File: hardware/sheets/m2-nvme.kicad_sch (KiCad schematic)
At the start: 20 parts, among them J50 M.2 M-key, M2 CM5002016 (J2), SW3 door microswitch, U50 TPS22965DSGR, U51 AP63203WU-7

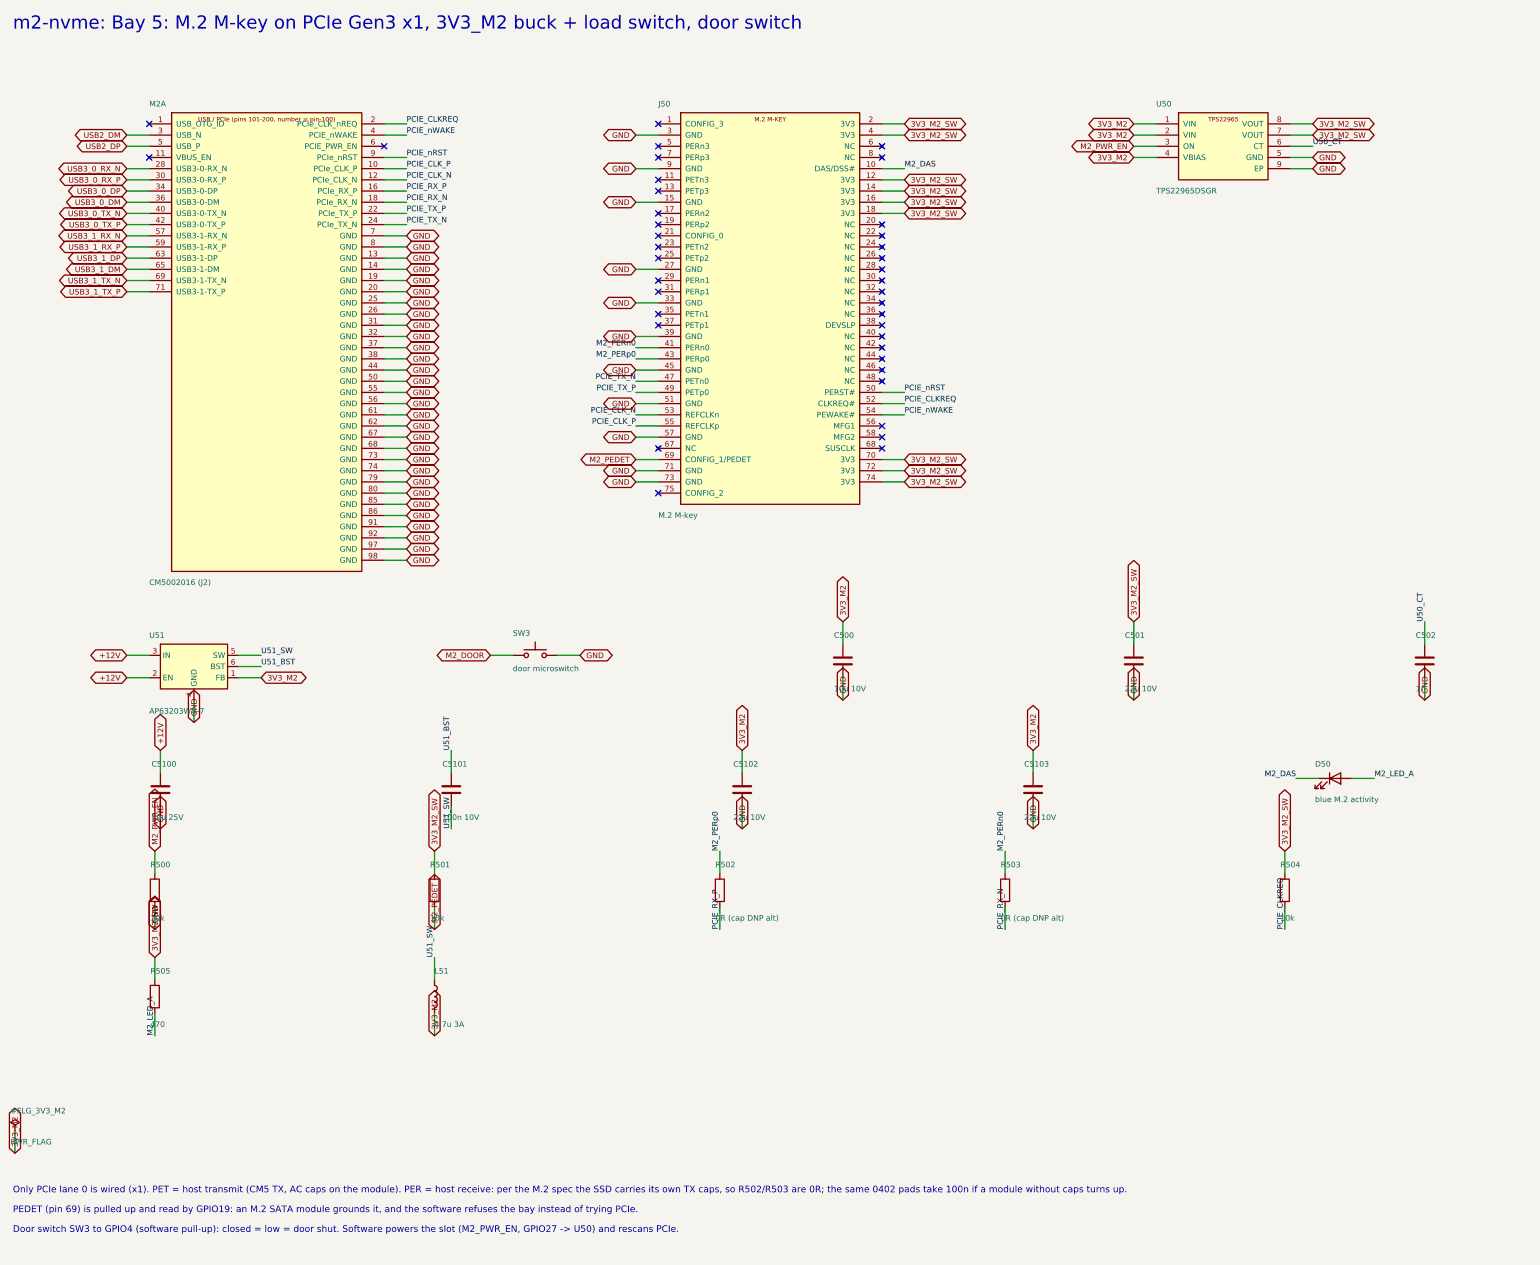
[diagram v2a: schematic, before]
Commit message: hardware: CM5 on the official 204-pad footprint, CM5IO M.2 footprint, reference-design fixes
From the Raspberry Pi CM5IO rev 2 KiCad files: single CM5 footprint with both
connectors and mounting holes; M.2 socket footprint; USB-C CC pins to the CM5;
fan PWM pull-up; microSD through a load switch on SD_PWR_ON; M.2 shield and
standoff pads to GND; PCIe polarity note. Board regenerated with the module
and M.2 at their real sizes; centre mounting hole dropped.

Co-Authored-By: Claude Fable 5.1 <noreply@anthropic.com>
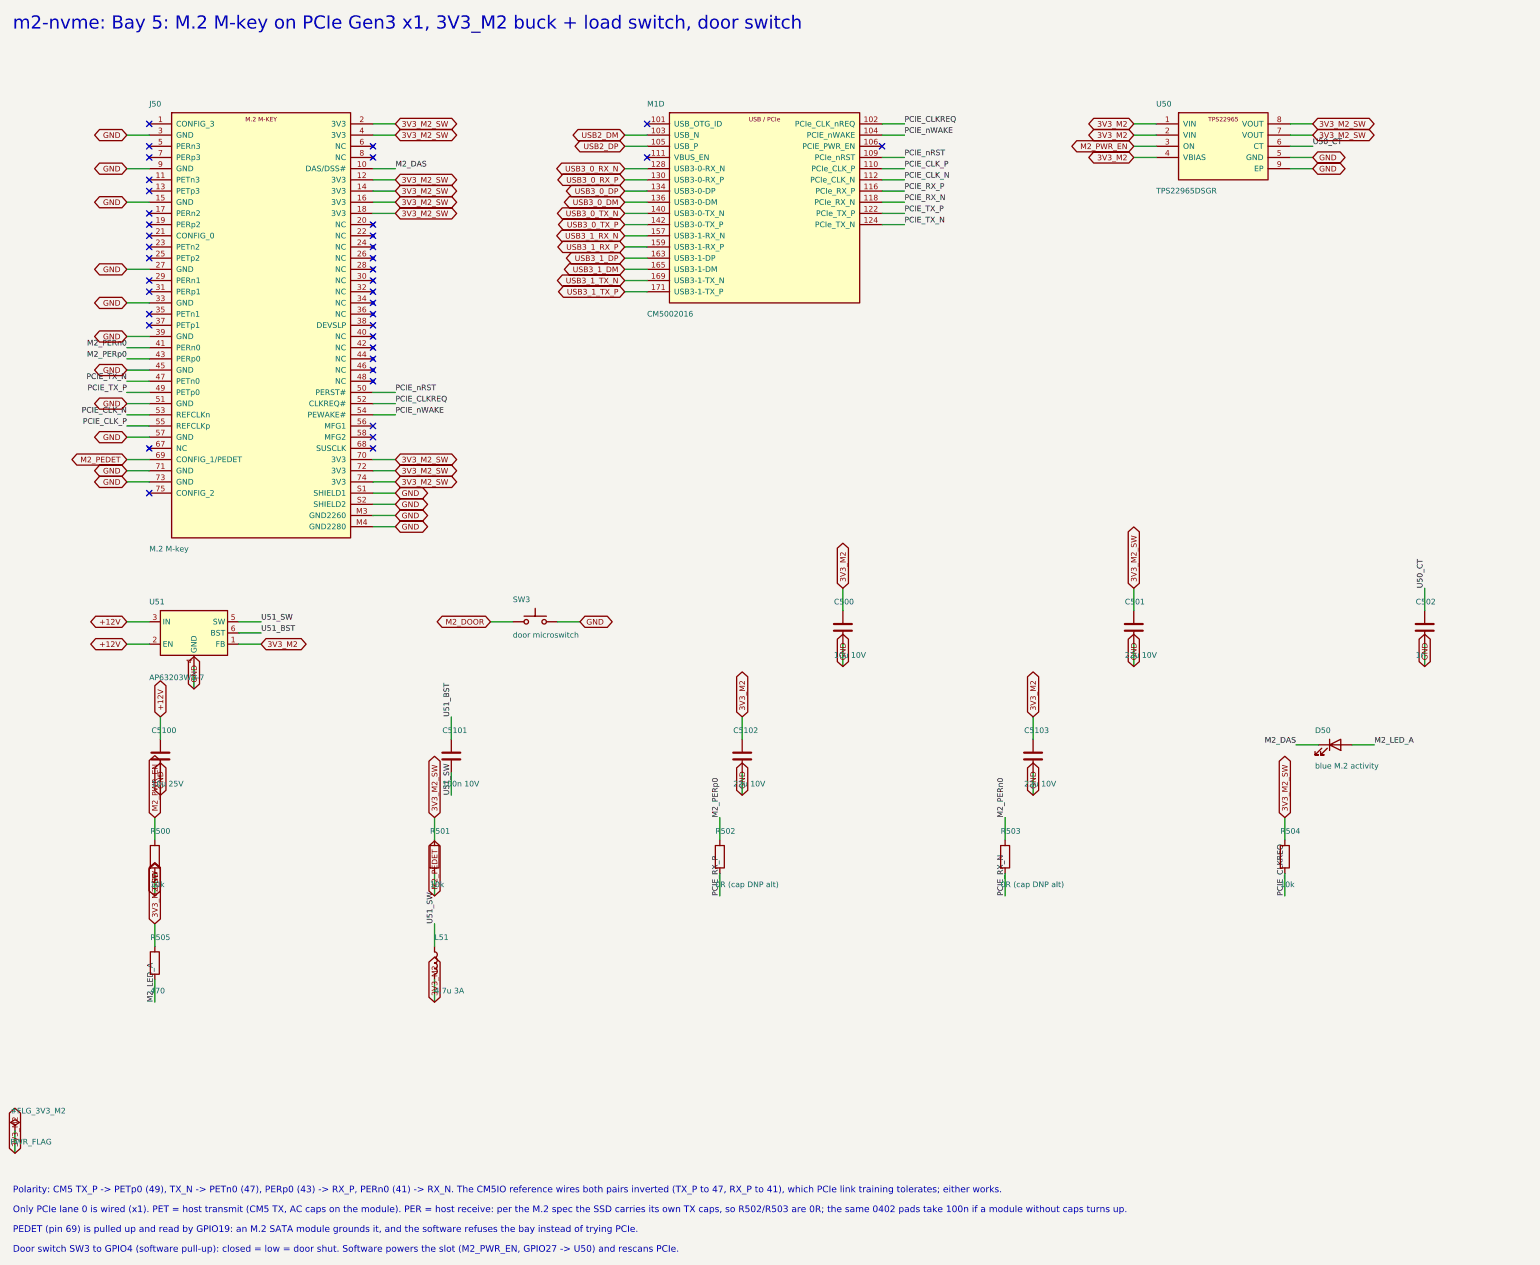
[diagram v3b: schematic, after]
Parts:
- J50: renamed from M2; value CM5002016 (J2) -> M.2 M-key; footprint Connector_Hirose_DF40:Hirose_DF40C-100DS-0.4V_2x50_P0.4mm -> brain-drain:M2_Socket3_MKey_CM5IO; symbol brain-drain:CM5_J2 -> brain-drain:M2_MKEY
- M1: renamed from J50; value M.2 M-key -> CM5002016; footprint brain-drain:M2_Socket3_MKey_4.2mm -> brain-drain:Raspberry-Pi-5-Compute-Module; symbol brain-drain:M2_MKEY -> brain-drain:CM5
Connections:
- net 3V3_M2_SW: now also J50.12 (3V3), J50.14 (3V3), J50.16 (3V3), J50.18 (3V3), J50.2 (3V3), J50.4 (3V3), J50.70 (3V3), J50.72 (3V3), J50.74 (3V3); no longer M1.12 (3V3), M1.14 (3V3), M1.16 (3V3), M1.18 (3V3), M1.2 (3V3), M1.4 (3V3), M1.70 (3V3), M1.72 (3V3), M1.74 (3V3)
- net GND: now also J50.15 (GND), J50.27 (GND), J50.3 (GND), J50.33 (GND), J50.39 (GND), J50.45 (GND), J50.51 (GND), J50.57 (GND), J50.71 (GND), J50.9 (GND), J50.M3 (GND2260), J50.M4 (GND2280), J50.S1 (SHIELD1), J50.S2 (SHIELD2); no longer J50.13 (GND), J50.14 (GND), J50.19 (GND), J50.20 (GND), J50.25 (GND), J50.26 (GND), J50.31 (GND), J50.32 (GND), J50.37 (GND), J50.38 (GND), J50.44 (GND), J50.50 (GND), J50.55 (GND), J50.56 (GND), J50.61 (GND), J50.62 (GND), J50.67 (GND), J50.68 (GND), J50.7 (GND), J50.74 (GND), J50.79 (GND), J50.8 (GND), J50.80 (GND), J50.85 (GND), J50.86 (GND), J50.91 (GND), J50.92 (GND), J50.97 (GND), J50.98 (GND), M1.15 (GND), M1.27 (GND), M1.3 (GND), M1.33 (GND), M1.39 (GND), M1.45 (GND), M1.51 (GND), M1.57 (GND), M1.71 (GND), M1.73 (GND), M1.9 (GND)
- net M2_DAS: now also J50.10 (DAS/DSS#); no longer M1.10 (DAS/DSS#)
- net M2_PEDET: now also J50.69 (CONFIG_1/PEDET); no longer M1.69 (CONFIG_1/PEDET)
- net M2_PERn0: now also J50.41 (PERn0); no longer M1.41 (PERn0)
- net M2_PERp0: now also J50.43 (PERp0); no longer M1.43 (PERp0)
- net PCIE_CLKREQ: now also J50.52 (CLKREQ#), M1.102 (PCIe_CLK_nREQ); no longer J50.2 (PCIe_CLK_nREQ), M1.52 (CLKREQ#)
- net PCIE_CLK_N: now also J50.53 (REFCLKn), M1.112 (PCIe_CLK_N); no longer J50.12 (PCIe_CLK_N), M1.53 (REFCLKn)
- net PCIE_CLK_P: now also J50.55 (REFCLKp), M1.110 (PCIe_CLK_P); no longer J50.10 (PCIe_CLK_P), M1.55 (REFCLKp)
- net PCIE_RX_N: now also M1.118 (PCIe_RX_N); no longer J50.18 (PCIe_RX_N)
- net PCIE_RX_P: now also M1.116 (PCIe_RX_P); no longer J50.16 (PCIe_RX_P)
- net PCIE_TX_N: now also J50.47 (PETn0), M1.124 (PCIe_TX_N); no longer J50.24 (PCIe_TX_N), M1.47 (PETn0)
- net PCIE_TX_P: now also J50.49 (PETp0), M1.122 (PCIe_TX_P); no longer J50.22 (PCIe_TX_P), M1.49 (PETp0)
- net PCIE_nRST: now also J50.50 (PERST#), M1.109 (PCIe_nRST); no longer J50.9 (PCIe_nRST), M1.50 (PERST#)
- net PCIE_nWAKE: now also J50.54 (PEWAKE#), M1.104 (PCIE_nWAKE); no longer J50.4 (PCIE_nWAKE), M1.54 (PEWAKE#)
- net USB2_DM: now also M1.103 (USB_N); no longer J50.3 (USB_N)
- net USB2_DP: now also M1.105 (USB_P); no longer J50.5 (USB_P)
- net USB3_0_DM: now also M1.136 (USB3-0-DM); no longer J50.36 (USB3-0-DM)
- net USB3_0_DP: now also M1.134 (USB3-0-DP); no longer J50.34 (USB3-0-DP)
- net USB3_0_RX_N: now also M1.128 (USB3-0-RX_N); no longer J50.28 (USB3-0-RX_N)
- net USB3_0_RX_P: now also M1.130 (USB3-0-RX_P); no longer J50.30 (USB3-0-RX_P)
- net USB3_0_TX_N: now also M1.140 (USB3-0-TX_N); no longer J50.40 (USB3-0-TX_N)
- net USB3_0_TX_P: now also M1.142 (USB3-0-TX_P); no longer J50.42 (USB3-0-TX_P)
- net USB3_1_DM: now also M1.165 (USB3-1-DM); no longer J50.65 (USB3-1-DM)
- net USB3_1_DP: now also M1.163 (USB3-1-DP); no longer J50.63 (USB3-1-DP)
- net USB3_1_RX_N: now also M1.157 (USB3-1-RX_N); no longer J50.57 (USB3-1-RX_N)
- net USB3_1_RX_P: now also M1.159 (USB3-1-RX_P); no longer J50.59 (USB3-1-RX_P)
- net USB3_1_TX_N: now also M1.169 (USB3-1-TX_N); no longer J50.69 (USB3-1-TX_N)
- net USB3_1_TX_P: now also M1.171 (USB3-1-TX_P); no longer J50.71 (USB3-1-TX_P)
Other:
- note added: "Polarity: CM5 TX_P -> PETp0 (49), TX_N -> PETn0 (47), PERp0 (43) -> RX_P, PERn0 (41) -> RX_N. The CM5IO reference wires both pairs inverted (TX_P to 47, RX_P to 41), which PCIe link training tolerates; either works."
- moved on the sheet: C500, C501, C502, C5100, C5101, C5102, C5103, D50, L51, R500, R501, R502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

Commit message: design v2: wireless brain box (C22-C23) — no Ethernet, no buzzer, passive cooler, hinged lid, Wi-Fi AP + QR + phone page, fabrication guide
hardware: 136x100 outline, CM5 wireless antenna edge on the left board edge with a copper-free
strip (rule area), DIN/USB-C/microSD on the right wall, M.2 along the front under the lid, lid
microswitch, CR2032 + service headers on the bottom; magjack and buzzer removed from the
netlist; check_place clean, DRC 0 errors; schematic + connections regenerated, render script
also exports the schematic
software: wifi.py (nmcli / simulated backends, ephemeral key, join, resets), webui.py (stdlib
HTTP phone page: status, certificates, log, join, reset), qr.py, OLED frames with the Wi-Fi QR
code, DIP mode 110 = SERVICE, braindrain wifi-reset; 74 tests, ruff clean; qrcode dependency
enclosure: hinged lid (rear knuckles, filament pin, front snap latch), vents on the antenna side
and front, right-wall cutouts, lid-open scene render
docs: C22/C23, FABRICATION.md (vendors, cost estimate, gates), STATUS R19-R20, panels rear/right,
OLED Wi-Fi mockup, README/ARCHITECTURE/USAGE/BOM/CHANGELOG/HISTORY/tracker updated

Co-Authored-By: Claude Fable 5.1 <noreply@anthropic.com>
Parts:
- SW3: value door microswitch -> lid microswitch
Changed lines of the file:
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@@
 			)
 		)
-		(property "Value" "door microswitch"
+		(property "Value" "lid microswitch"
 			(at 143.51 149.058 0)
 			(effects

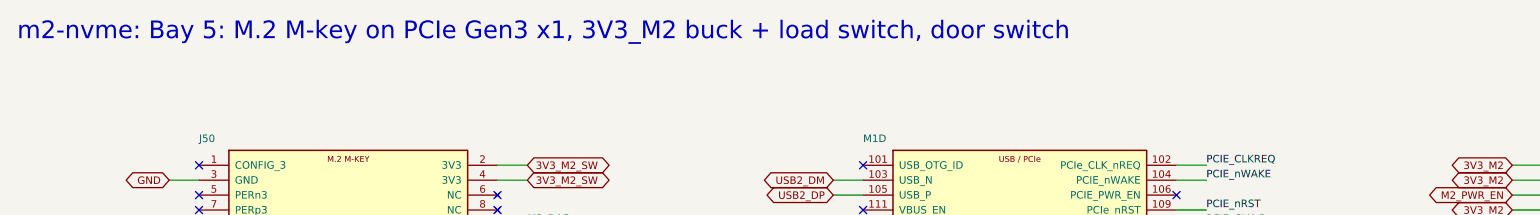
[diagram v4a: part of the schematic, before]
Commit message: docs: C24 brain + bay cards — decisions, architecture, BOM card table, fabrication, README, USAGE, STATUS, changelog, history; diagrams: 8 slots, lid plan, left wall
Co-Authored-By: Claude Fable 5.1 <noreply@anthropic.com>
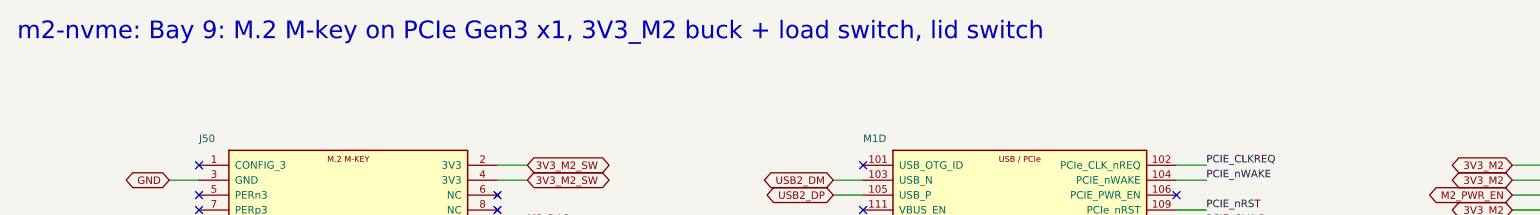
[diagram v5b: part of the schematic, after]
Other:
- note added: "m2-nvme: Bay 9: M.2 M-key on PCIe Gen3 x1, 3V3_M2 buck + load switch, lid switch"
- note removed: "m2-nvme: Bay 5: M.2 M-key on PCIe Gen3 x1, 3V3_M2 buck + load switch, door switch"
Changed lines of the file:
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@@
 		(company "brain-drain")
 	)
-	(text "m2-nvme: Bay 5: M.2 M-key on PCIe Gen3 x1, 3V3_M2 buck + load switch, door switch"
+	(text "m2-nvme: Bay 9: M.2 M-key on PCIe Gen3 x1, 3V3_M2 buck + load switch, lid switch"
 		(exclude_from_sim no)
 		(at 30 12 0)
@@
 		(instances
 			(project "brain-drain"
-				(path "/0b6a1e2a-0000-4000-8000-000000000001/0b6a1e2a-0000-4000-8000-000000000015"
+				(path "/0b6a1e2a-0000-4000-8000-000000000001/0b6a1e2a-0000-4000-8000-000000000008"
 					(reference "J50")
 					(unit 1)
@@
 		(instances
 			(project "brain-drain"
-				(path "/0b6a1e2a-0000-4000-8000-000000000001/0b6a1e2a-0000-4000-8000-000000000015"
+				(path "/0b6a1e2a-0000-4000-8000-000000000001/0b6a1e2a-0000-4000-8000-000000000008"
 					(reference "M1")
 					(unit 4)
@@
 		(instances
 			(project "brain-drain"
-				(path "/0b6a1e2a-0000-4000-8000-000000000001/0b6a1e2a-0000-4000-8000-000000000015"
+				(path "/0b6a1e2a-0000-4000-8000-000000000001/0b6a1e2a-0000-4000-8000-000000000008"
 					(reference "U50")
 					(unit 1)
@@
 		(instances
 			(project "brain-drain"
-				(path "/0b6a1e2a-0000-4000-8000-000000000001/0b6a1e2a-0000-4000-8000-000000000015"
+				(path "/0b6a1e2a-0000-4000-8000-000000000001/0b6a1e2a-0000-4000-8000-000000000008"
 					(reference "U51")
 					(unit 1)
@@
 		(instances
 			(project "brain-drain"
-				(path "/0b6a1e2a-0000-4000-8000-000000000001/0b6a1e2a-0000-4000-8000-000000000015"
+				(path "/0b6a1e2a-0000-4000-8000-000000000001/0b6a1e2a-0000-4000-8000-000000000008"
 					(reference "SW3")
 					(unit 1)
@@
 		(instances
 			(project "brain-drain"
-				(path "/0b6a1e2a-0000-4000-8000-000000000001/0b6a1e2a-0000-4000-8000-000000000015"
+				(path "/0b6a1e2a-0000-4000-8000-000000000001/0b6a1e2a-0000-4000-8000-000000000008"
 					(reference "C500")
 					(unit 1)
@@
 		(instances
 			(project "brain-drain"
-				(path "/0b6a1e2a-0000-4000-8000-000000000001/0b6a1e2a-0000-4000-8000-000000000015"
+				(path "/0b6a1e2a-0000-4000-8000-000000000001/0b6a1e2a-0000-4000-8000-000000000008"
 					(reference "C501")
 					(unit 1)
@@
 		(instances
 			(project "brain-drain"
-				(path "/0b6a1e2a-0000-4000-8000-000000000001/0b6a1e2a-0000-4000-8000-000000000015"
+				(path "/0b6a1e2a-0000-4000-8000-000000000001/0b6a1e2a-0000-4000-8000-000000000008"
 					(reference "C502")
 					(unit 1)
@@
 		(instances
 			(project "brain-drain"
-				(path "/0b6a1e2a-0000-4000-8000-000000000001/0b6a1e2a-0000-4000-8000-000000000015"
+				(path "/0b6a1e2a-0000-4000-8000-000000000001/0b6a1e2a-0000-4000-8000-000000000008"
 					(reference "C5100")
 					(unit 1)
@@
 		(instances
 			(project "brain-drain"
-				(path "/0b6a1e2a-0000-4000-8000-000000000001/0b6a1e2a-0000-4000-8000-000000000015"
+				(path "/0b6a1e2a-0000-4000-8000-000000000001/0b6a1e2a-0000-4000-8000-000000000008"
 					(reference "C5101")
 					(unit 1)
@@
 		(instances
 			(project "brain-drain"
-				(path "/0b6a1e2a-0000-4000-8000-000000000001/0b6a1e2a-0000-4000-8000-000000000015"
+				(path "/0b6a1e2a-0000-4000-8000-000000000001/0b6a1e2a-0000-4000-8000-000000000008"
 					(reference "C5102")
 					(unit 1)
@@
 		(instances
 			(project "brain-drain"
-				(path "/0b6a1e2a-0000-4000-8000-000000000001/0b6a1e2a-0000-4000-8000-000000000015"
+				(path "/0b6a1e2a-0000-4000-8000-000000000001/0b6a1e2a-0000-4000-8000-000000000008"
 					(reference "C5103")
 					(unit 1)
@@
 		(instances
 			(project "brain-drain"
-				(path "/0b6a1e2a-0000-4000-8000-000000000001/0b6a1e2a-0000-4000-8000-000000000015"
+				(path "/0b6a1e2a-0000-4000-8000-000000000001/0b6a1e2a-0000-4000-8000-000000000008"
 					(reference "D50")
 					(unit 1)
@@
 		(instances
 			(project "brain-drain"
-				(path "/0b6a1e2a-0000-4000-8000-000000000001/0b6a1e2a-0000-4000-8000-000000000015"
+				(path "/0b6a1e2a-0000-4000-8000-000000000001/0b6a1e2a-0000-4000-8000-000000000008"
 					(reference "R500")
 					(unit 1)
@@
 		(instances
 			(project "brain-drain"
-				(path "/0b6a1e2a-0000-4000-8000-000000000001/0b6a1e2a-0000-4000-8000-000000000015"
+				(path "/0b6a1e2a-0000-4000-8000-000000000001/0b6a1e2a-0000-4000-8000-000000000008"
 					(reference "R501")
 					(unit 1)
@@
 		(instances
 			(project "brain-drain"
-				(path "/0b6a1e2a-0000-4000-8000-000000000001/0b6a1e2a-0000-4000-8000-000000000015"
+				(path "/0b6a1e2a-0000-4000-8000-000000000001/0b6a1e2a-0000-4000-8000-000000000008"
 					(reference "R502")
 					(unit 1)
@@
 		(instances
 			(project "brain-drain"
-				(path "/0b6a1e2a-0000-4000-8000-000000000001/0b6a1e2a-0000-4000-8000-000000000015"
+				(path "/0b6a1e2a-0000-4000-8000-000000000001/0b6a1e2a-0000-4000-8000-000000000008"
 					(reference "R503")
 					(unit 1)
@@
 		(instances
 			(project "brain-drain"
-				(path "/0b6a1e2a-0000-4000-8000-000000000001/0b6a1e2a-0000-4000-8000-000000000015"
+				(path "/0b6a1e2a-0000-4000-8000-000000000001/0b6a1e2a-0000-4000-8000-000000000008"
 					(reference "R504")
 					(unit 1)
@@
 		(instances
 			(project "brain-drain"
-				(path "/0b6a1e2a-0000-4000-8000-000000000001/0b6a1e2a-0000-4000-8000-000000000015"
+				(path "/0b6a1e2a-0000-4000-8000-000000000001/0b6a1e2a-0000-4000-8000-000000000008"
 					(reference "R505")
 					(unit 1)
@@
 		(instances
 			(project "brain-drain"
-				(path "/0b6a1e2a-0000-4000-8000-000000000001/0b6a1e2a-0000-4000-8000-000000000015"
+				(path "/0b6a1e2a-0000-4000-8000-000000000001/0b6a1e2a-0000-4000-8000-000000000008"
 					(reference "L51")
 					(unit 1)
@@
 		(instances
 			(project "brain-drain"
-				(path "/0b6a1e2a-0000-4000-8000-000000000001/0b6a1e2a-0000-4000-8000-000000000015"
+				(path "/0b6a1e2a-0000-4000-8000-000000000001/0b6a1e2a-0000-4000-8000-000000000008"
 					(reference "#FLG_3V3_M2")
 					(unit 1)
